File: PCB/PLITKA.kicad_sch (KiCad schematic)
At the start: 48 parts, among them SW1 MX_SW_HS, SW10 MX_SW_HS, SW11 MX_SW_HS, SW12 MX_SW_HS, SW13 MX_SW_HS, SW14 MX_SW_HS, SW15 MX_SW_HS, SW16 MX_SW_HS, SW17 MX_SW_HS, SW2 MX_SW_HS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

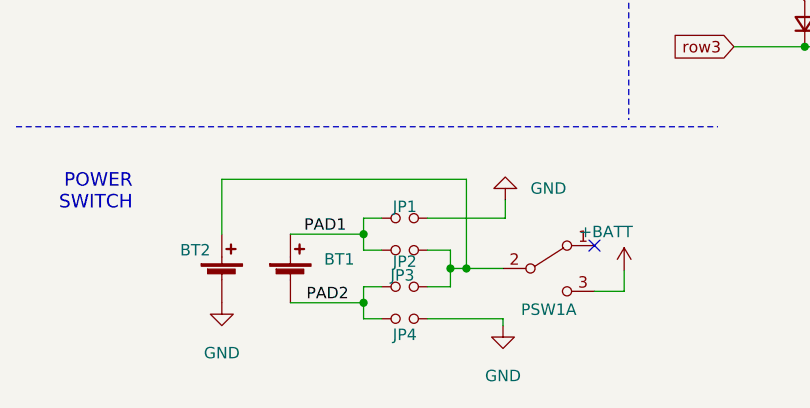
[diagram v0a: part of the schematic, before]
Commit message: Non-JSC battery connection removed
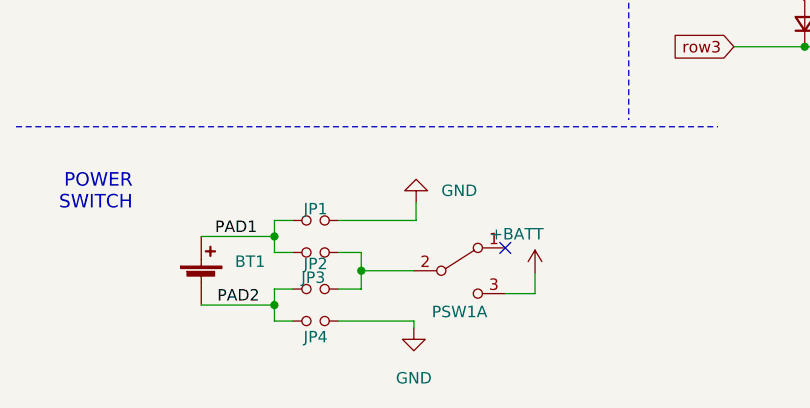
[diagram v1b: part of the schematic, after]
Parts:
- removed BT2: Battery_Cell, PLITKA:custombatteryconnector, symbol Device:Battery_Cell
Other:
- moved on the sheet: BT1, JP1, JP2, JP3, JP4, PSW1A
